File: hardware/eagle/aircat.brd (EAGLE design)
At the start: 53.2 x 59.6 mm, 154 parts, among them CON1 A10_OLINUXINO_LIME_SHIELD_TEM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, U1 PCM3168APAP, U2 OPA1644AIPW, U3 OPA1644AIPW, U4 OPA1644AIPW, U6 LM2662M

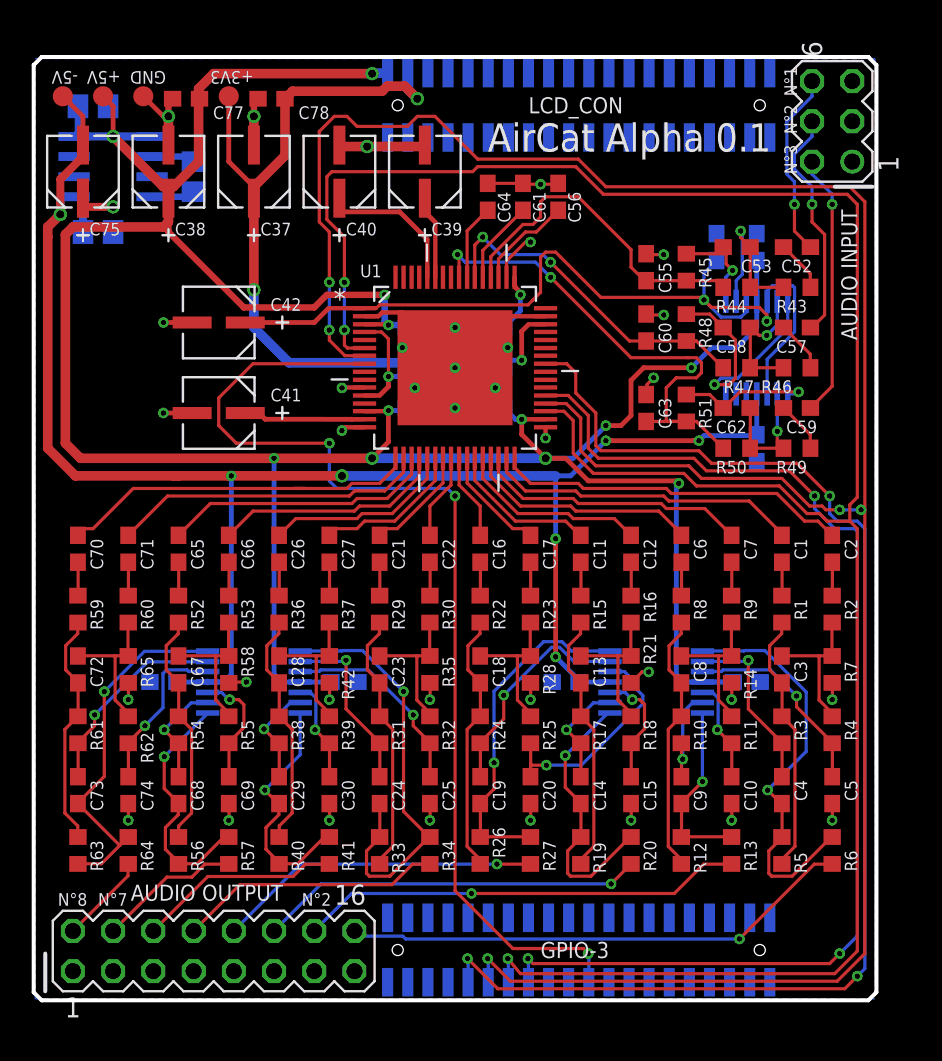
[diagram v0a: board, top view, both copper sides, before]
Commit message: pads added for unused pins
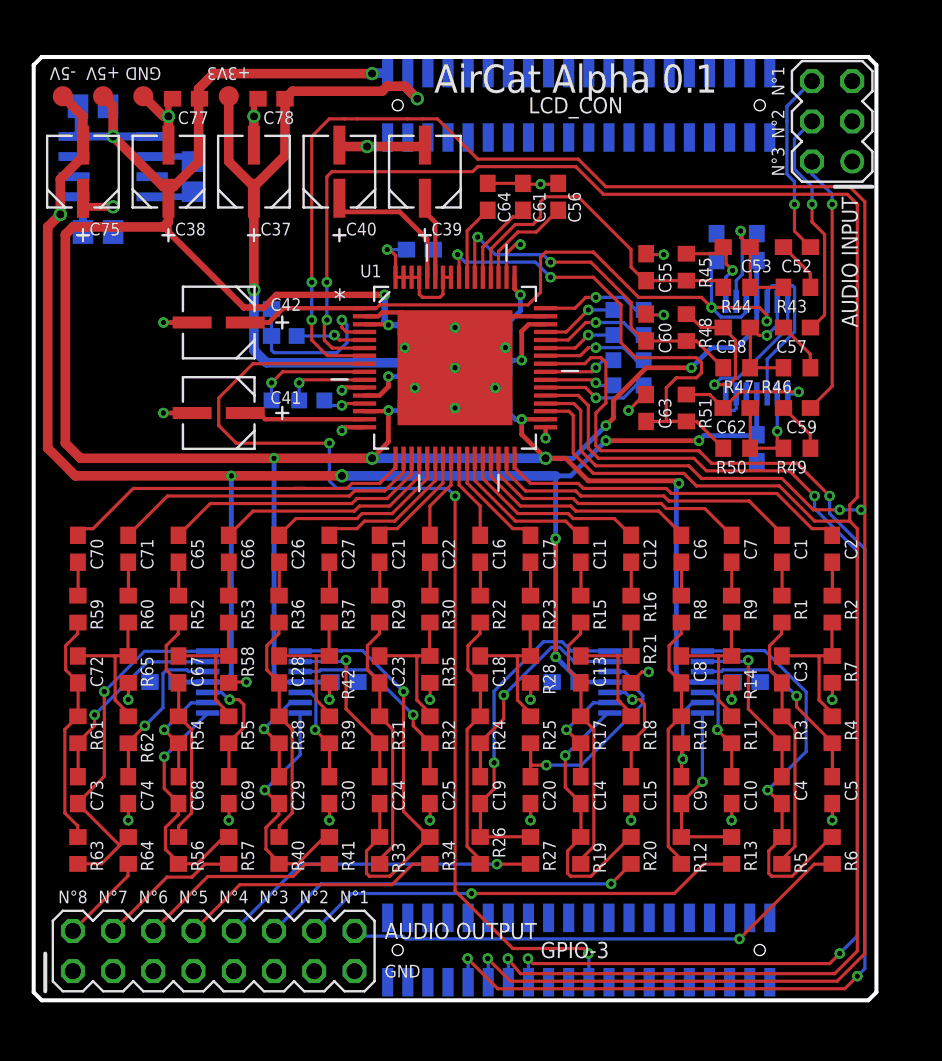
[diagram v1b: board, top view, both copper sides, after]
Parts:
- added C76: 0.001-1µF, rcl:C0603
- added DIN2, DIN3, DIN4, DOUT2, DOUT3, MC, MDI, MDO, MODE, MS, OVF, ZERO: -5V, testpad:TP10SQ
- added RST: 0 Ohm, rcl:R0603
- SV1: device con-lstb:MA03-2 -> con-lstb-without-pin-numbers:MA03-2
- SV2: value AUDIO OUTPUT -> (none); device con-lstb:MA08-2 -> con-lstb-without-pin-numbers:MA08-2
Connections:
- removed net AOP_IN_L+: U4.12
- removed net AOP_IN_L-: U4.13
- removed net DIN3(N/C): CON1.3-18
- removed net DIN4(N/C): CON1.3-20
- removed net N$42: U1.43
- removed net N$43: U1.44
- removed net VIN4+: U1.57
- removed net VIN4-: U1.58
- removed net VIN5+: U1.62
- removed net VIN5-: U1.61
- removed net VIN6+: U1.64
- removed net VIN6-: U1.63
- new net MC: MC.TP, U1.42
- new net MDI: MDI.TP, U1.43
- new net MDO: MDO.TP, U1.44
- new net MODE: MODE.TP, U1.48
- new net MS: MS.TP, U1.45
- new net OVF: OVF.TP, U1.5
- new net VIN4-6: C76.1, U1.57, U1.58, U1.61, U1.62, U1.63, U1.64
- new net ZERO: U1.13, ZERO.TP
- net +3V3: now also RST.1, RST.2
- net AOP_OUT_L: now also U4.13
- net DIN2: now also DIN2.TP
- net DIN3: now also DIN3.TP
- net DIN4: now also DIN4.TP
- net DOUT2: now also DOUT2.TP
- net DOUT3: now also DOUT3.TP
- net GND: now also C76.2, U4.12
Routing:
- net VIN4-6: track 0.00 -> 9.09 mm, vias 0 -> 1
- net +3V3: track 63.4 -> 72.1 mm, vias 4 -> 5
- net DOUT2: track 0.00 -> 7.27 mm, vias 0 -> 1
- net MDO: track 0.00 -> 6.98 mm, vias 0 -> 1
- net MODE: track 0.00 -> 6.80 mm, vias 0 -> 1
- net DIN2: track 0.00 -> 6.79 mm, vias 0 -> 1
- net MC: track 0.00 -> 6.73 mm, vias 0 -> 1
- net DOUT3: track 0.00 -> 5.32 mm, vias 0 -> 1
- net MS: track 0.00 -> 4.86 mm, vias 0 -> 1
- net MDI: track 0.00 -> 4.63 mm, vias 0 -> 1
- net DIN4: track 0.00 -> 4.59 mm, vias 0 -> 1
- net OVF: track 0.00 -> 4.44 mm, vias 0 -> 1
- net DIN3: track 0.00 -> 4.43 mm, vias 0 -> 1
- net ZERO: track 0.00 -> 2.82 mm, vias 0 -> 1
- net AOP_OUT_L: track 0.00 -> 2.61 mm
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
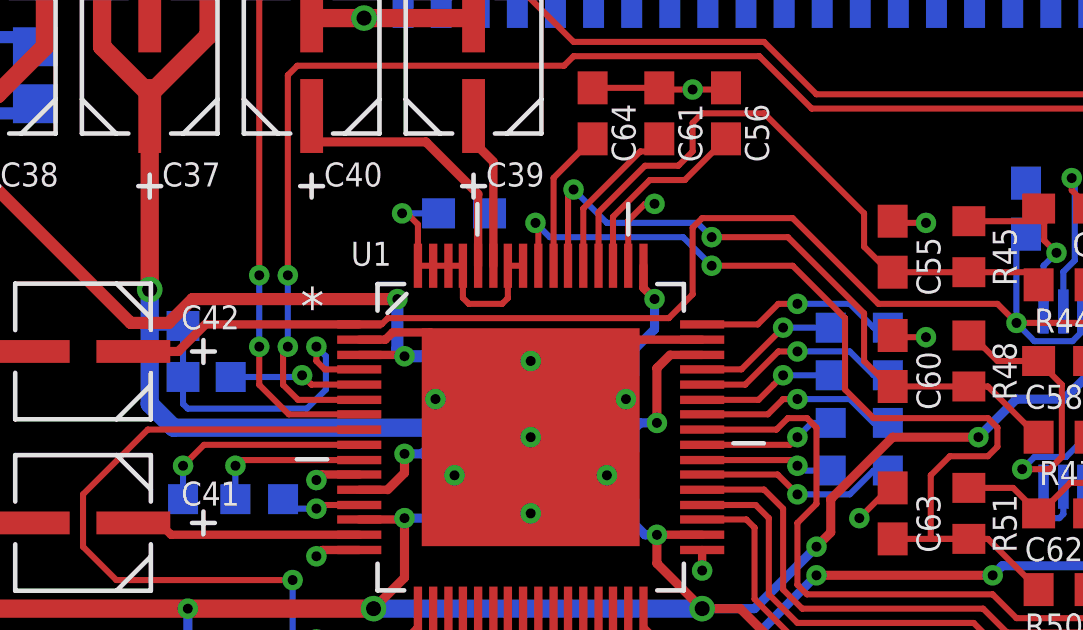
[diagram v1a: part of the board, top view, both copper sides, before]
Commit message: Mode pin connection ok (VDD+pulldown)
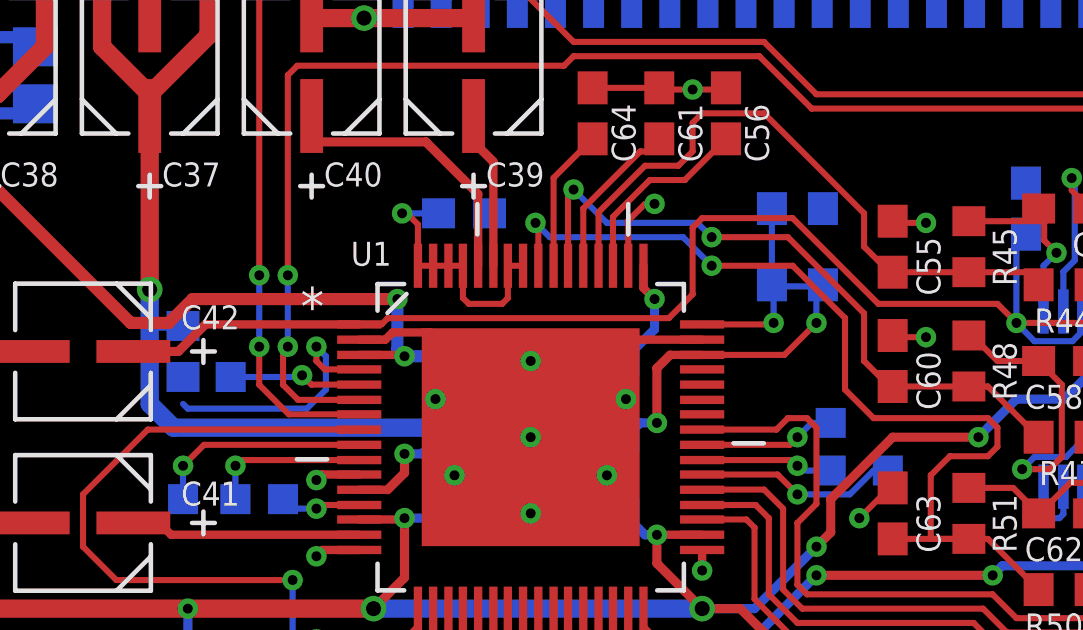
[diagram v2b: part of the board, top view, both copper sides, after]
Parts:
- removed MC, MDI, MDO, MS: -5V, testpad:TP10SQ
- added R66: 220k, rcl:R0603
- DIN2, DIN3, DIN4, DOUT2, DOUT3, ZERO: value -5V -> (none)
- MODE: value -5V -> 0 Ohm; device testpad:TP10SQ -> rcl:R0603
- moved MODE 3.34 mm to (8.89, 15.2)
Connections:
- removed net MODE: MODE.TP, U1.48
- net +3V3: now also MODE.1, MODE.2, R66.2, U1.48
- net GND: now also R66.1
- net MC: now also CON1.3-28; no longer MC.TP
- net MDI: now also CON1.3-30; no longer MDI.TP
- net MDO: now also CON1.3-32; no longer MDO.TP
- net MS: now also CON1.3-26; no longer MS.TP
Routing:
- net +3V3: track 72.1 -> 83.3 mm, vias 5 -> 7
- net MDO: track 6.98 -> 0.00 mm, vias 1 -> 0
- net MODE: track 6.80 -> 0.00 mm, vias 1 -> 0
- net MC: track 6.73 -> 0.00 mm, vias 1 -> 0
- net MS: track 4.86 -> 0.00 mm, vias 1 -> 0
- net MDI: track 4.63 -> 0.00 mm, vias 1 -> 0

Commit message: all data lines connected
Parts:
- moved C63 2.91 mm to (13.5, 10.2), turned to 90 degrees
- moved C60 2.84 mm to (13.3, 15.2)
- moved C57 2.84 mm to (22.9, 15.2)
- moved C58 2.84 mm to (19.1, 15.2)
- moved R43 2.84 mm to (22.9, 17.8)
- moved R44 2.84 mm to (19.1, 17.8)
- moved R48 2.84 mm to (15.9, 15.2)
- moved U4 2.84 mm to (20.3, 14.0)
- moved C55 2.84 mm to (13.3, 19.1)
- moved C51 2.84 mm to (20.3, 7.62)
- moved C59 2.84 mm to (22.9, 10.2)
- moved C62 2.84 mm to (19.1, 10.2)
- moved R49 2.84 mm to (22.9, 7.62)
- moved R50 2.84 mm to (19.1, 7.62)
- moved R51 2.84 mm to (15.9, 10.2)
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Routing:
- net MS: track 0.00 -> 57.9 mm, vias 0 -> 3
- net MDO: track 0.00 -> 46.6 mm, vias 0 -> 3
- net MDI: track 0.00 -> 45.5 mm, vias 0 -> 3
- net MC: track 0.00 -> 44.3 mm, vias 0 -> 3
- net -5V: track 109.4 -> 124.2 mm
- net GND: track 62.6 -> 77.1 mm, vias 37 -> 38
- net +3V3: track 83.3 -> 86.7 mm
- net ANALOG_IN_2: track 14.7 -> 12.0 mm
- net ANALOG_IN_3: track 16.7 -> 14.3 mm
- net VIN3+: track 33.3 -> 31.1 mm
- net N$12: track 9.47 -> 11.6 mm
- net BCKAD/DA: track 152.7 -> 150.9 mm
- net DIN3: track 4.43 -> 5.99 mm
- net LRCKAD/DA: track 143.5 -> 142.0 mm, vias 3 -> 5
- net SCKI: track 84.3 -> 83.2 mm
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
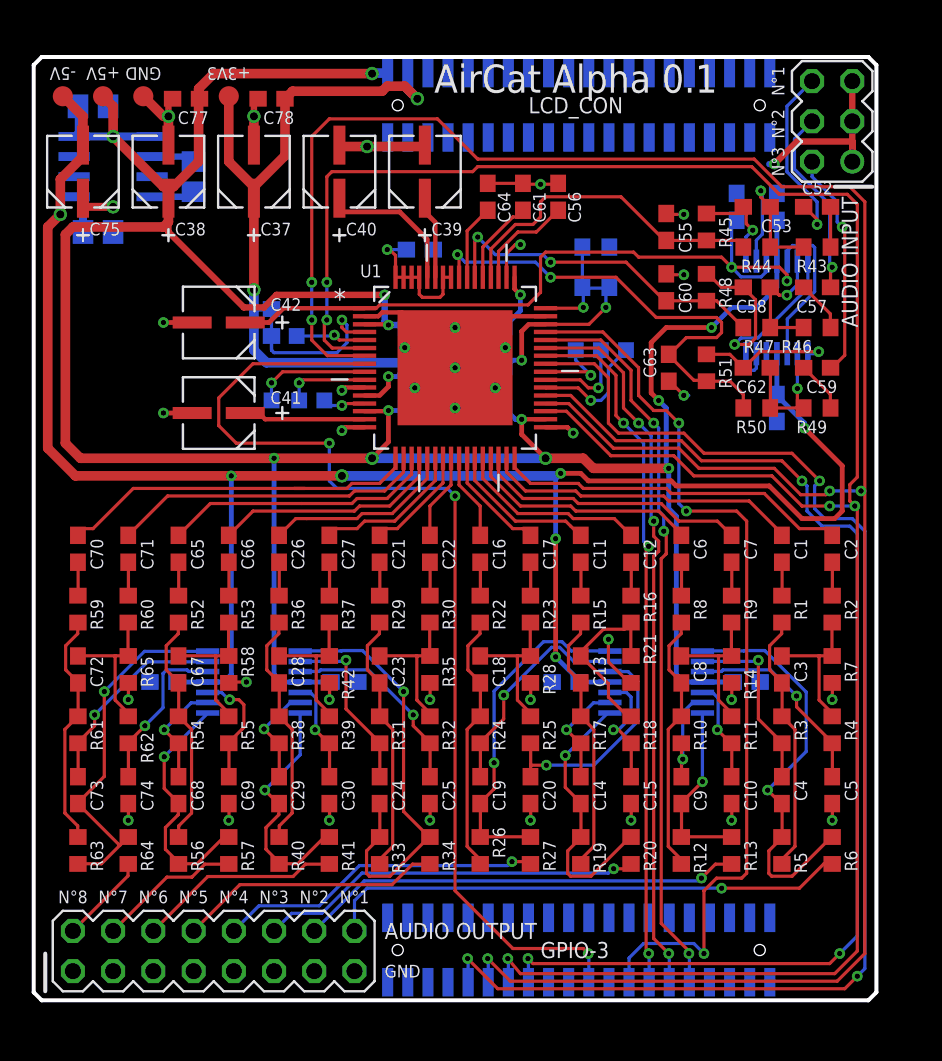
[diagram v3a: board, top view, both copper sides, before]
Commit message: componant labels better placed
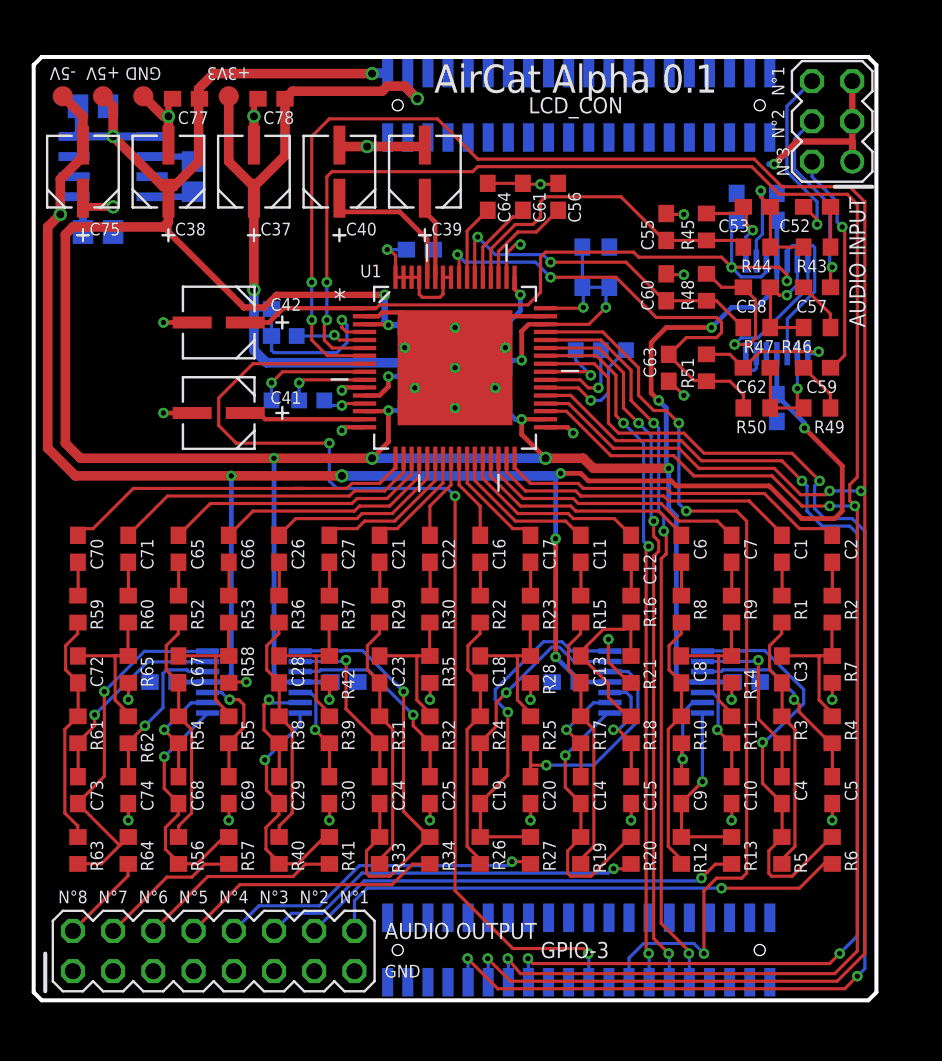
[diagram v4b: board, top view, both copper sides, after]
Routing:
- net AOP_IN_F-: track 6.43 -> 7.52 mm
- net AOP_OUT_D: track 21.6 -> 22.3 mm
